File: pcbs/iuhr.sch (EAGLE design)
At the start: 70 parts, among them IC1 TPS77033, IC2 MEGA48/88/168-AU, Q1 20.000MHz

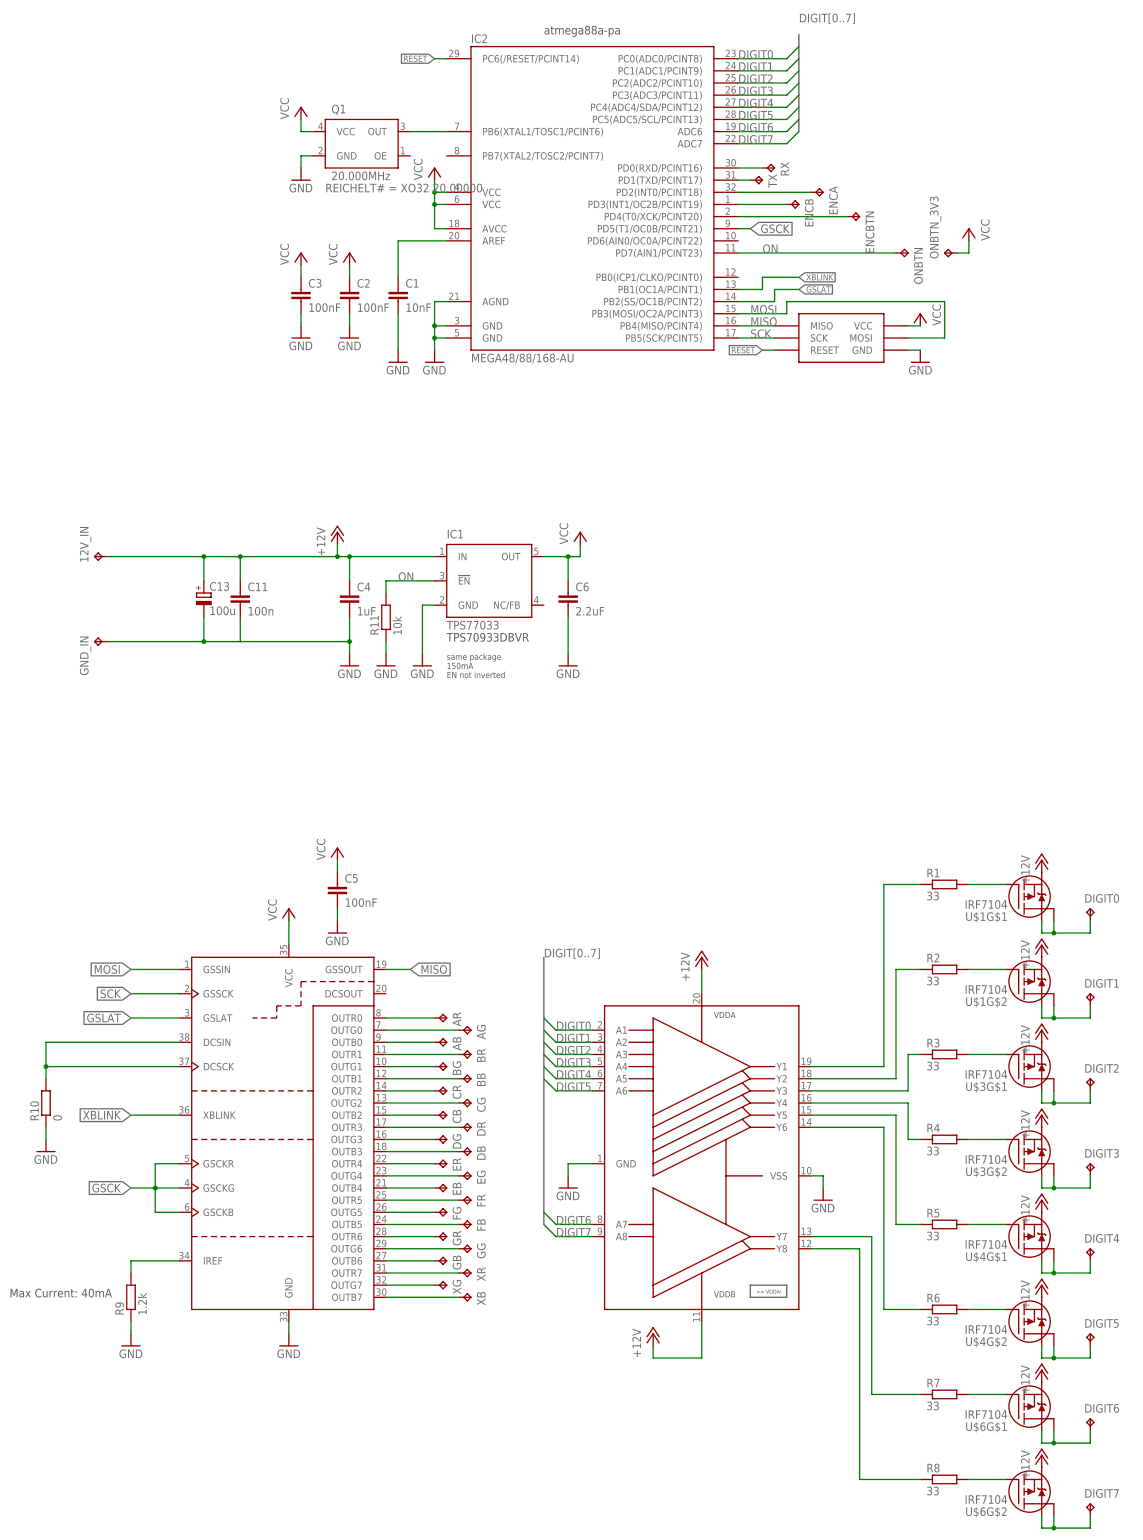
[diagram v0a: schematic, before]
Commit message: Started board layout
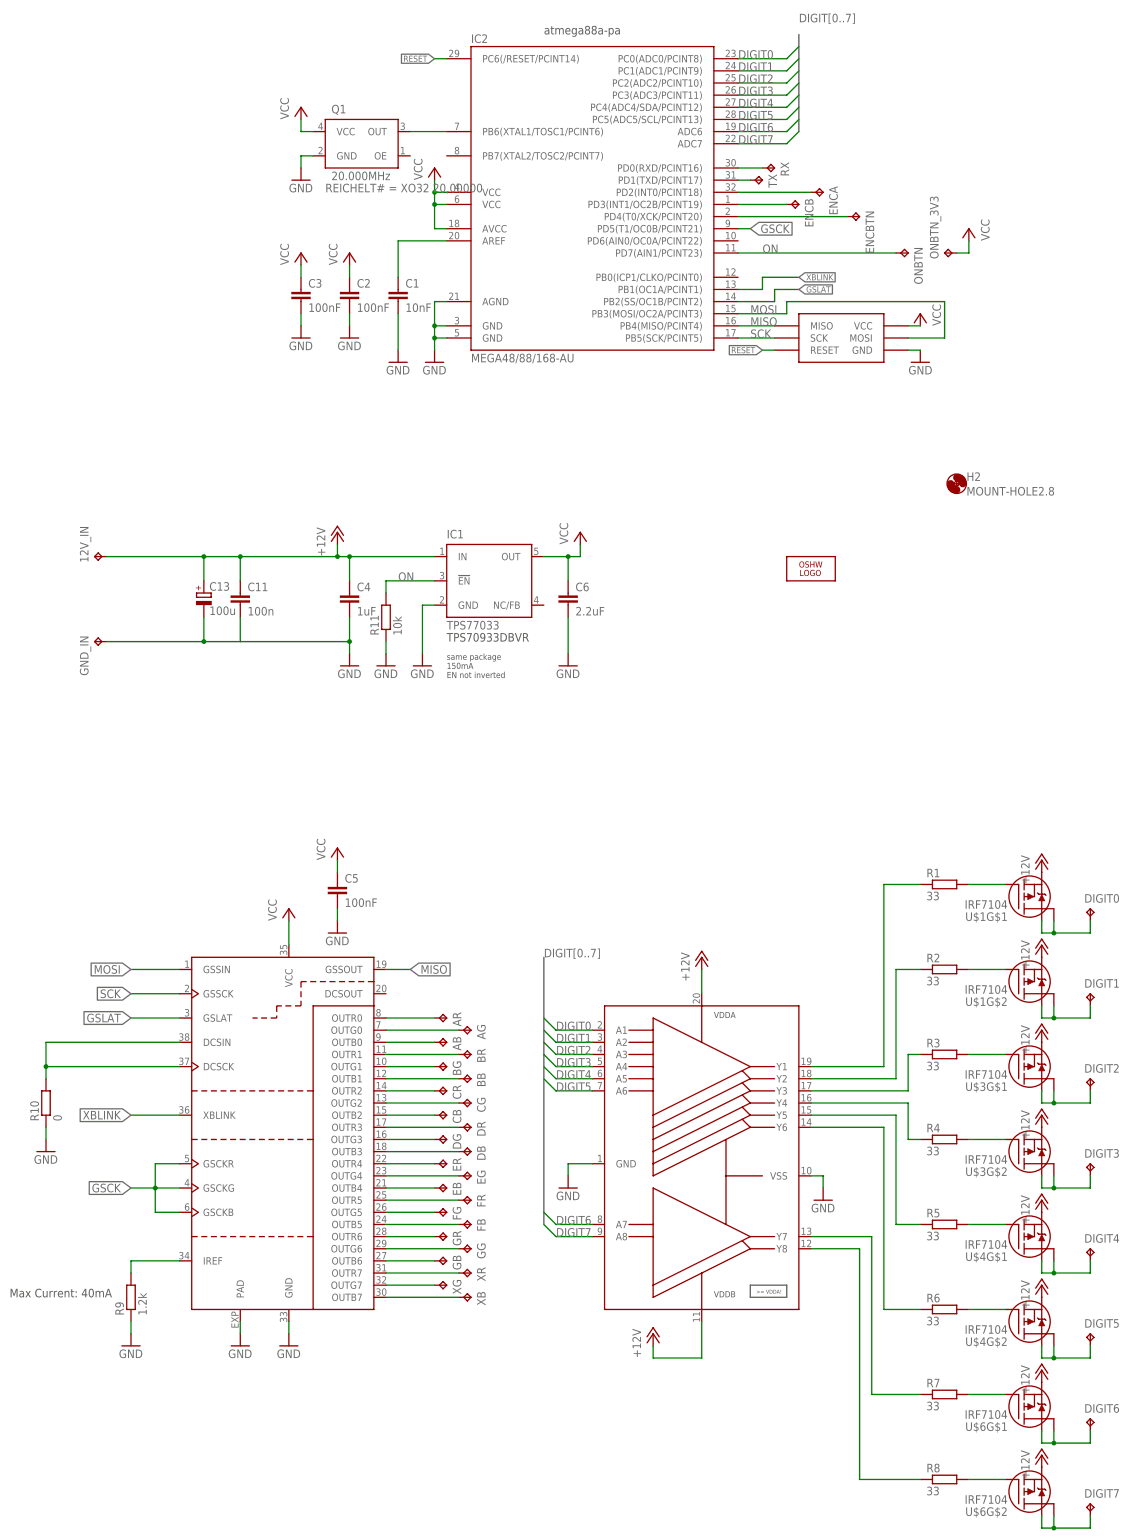
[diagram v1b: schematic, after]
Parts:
- added H2: MOUNT-HOLE2.8, holes:MOUNT-HOLE2.8
- added LOGO2: OSHW_LOGO_8MILX0150-NT, ea:OSHW_LOGO_8MILX0150-NT
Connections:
- net GND: now also DAP1.PAD
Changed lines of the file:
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@@
 <part name="P+20" library="supply1" deviceset="VCC" device=""/>
 <part name="GND15" library="supply1" deviceset="GND" device=""/>
+<part name="H2" library="holes" deviceset="MOUNT-HOLE" device="2.8"/>
+<part name="GND16" library="supply1" deviceset="GND" device=""/>
+<part name="LOGO2" library="ea" deviceset="OSHW_LOGO_8MIL" device="X0150-NT"/>
 </parts>
 <sheets>
@@
 <instance part="P+20" gate="VCC" x="88.9" y="-12.7"/>
 <instance part="GND15" gate="1" x="88.9" y="-30.48"/>
+<instance part="H2" gate="G$1" x="218.44" y="63.5"/>
+<instance part="GND16" gate="1" x="68.58" y="-116.84"/>
+<instance part="LOGO2" gate="G$1" x="187.96" y="45.72"/>
 </instances>
 <busses>
@@
 <wire x1="88.9" y1="-27.94" x2="88.9" y2="-25.4" width="0.1524" layer="91"/>
 </segment>
+<segment>
+<pinref part="DAP1" gate="G$1" pin="PAD"/>
+<pinref part="GND16" gate="1" pin="GND"/>
+<wire x1="68.58" y1="-114.3" x2="68.58" y2="-111.76" width="0.1524" layer="91"/>
+</segment>
 </net>

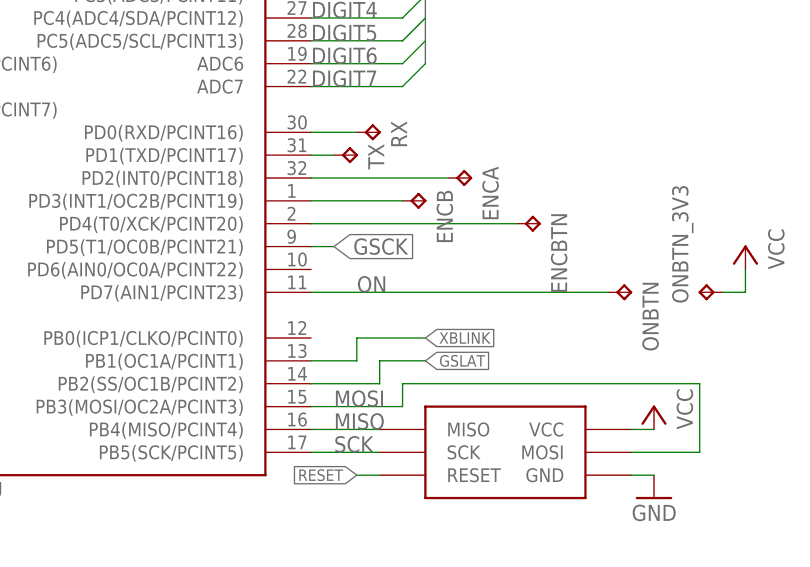
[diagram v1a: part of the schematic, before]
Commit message: No Airwires. No unapproved DRC Errors.
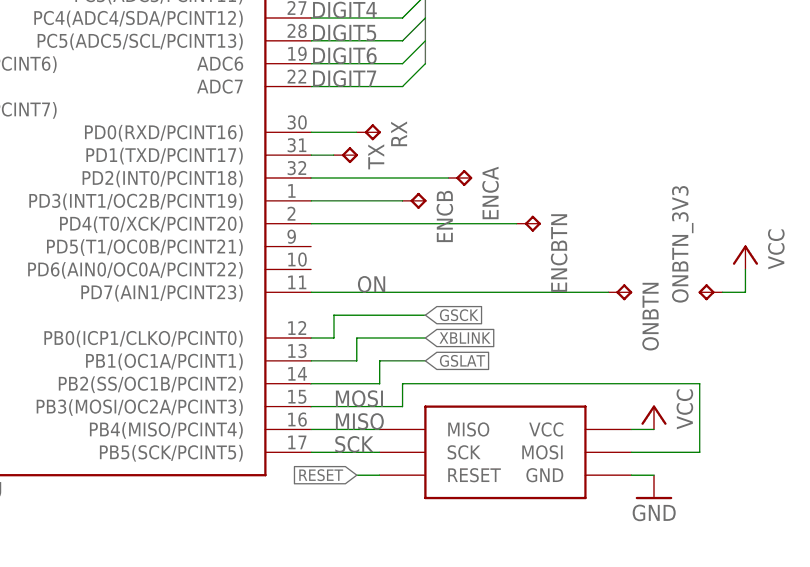
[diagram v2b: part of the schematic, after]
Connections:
- net GSCK: now also IC2.PB0(ICP1/CLKO/PCINT0); no longer IC2.PD5(T1/OC0B/PCINT21)
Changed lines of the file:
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@@
 </segment>
 <segment>
-<pinref part="IC2" gate="1" pin="PD5(T1/OC0B/PCINT21)"/>
-<wire x1="172.72" y1="116.84" x2="175.26" y2="116.84" width="0.1524" layer="91"/>
-<label x="175.26" y="116.84" size="1.778" layer="95" xref="yes"/>
+<pinref part="IC2" gate="1" pin="PB0(ICP1/CLKO/PCINT0)"/>
+<wire x1="172.72" y1="106.68" x2="175.26" y2="106.68" width="0.1524" layer="91"/>
+<wire x1="175.26" y1="106.68" x2="175.26" y2="109.22" width="0.1524" layer="91"/>
+<wire x1="175.26" y1="109.22" x2="185.42" y2="109.22" width="0.1524" layer="91"/>
+<label x="185.42" y="109.22" size="1.27" layer="95" xref="yes"/>
 </segment>
 </net>

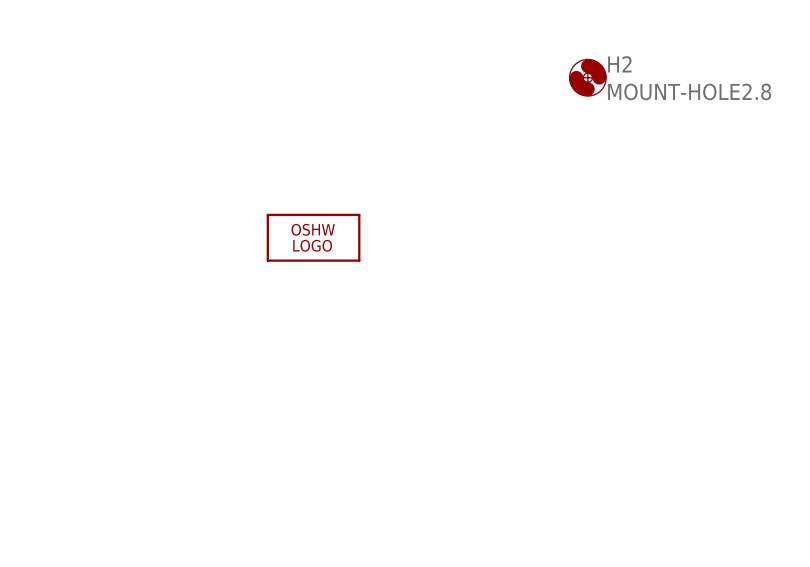
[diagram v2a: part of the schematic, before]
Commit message: Add ground plane and thermal vias.
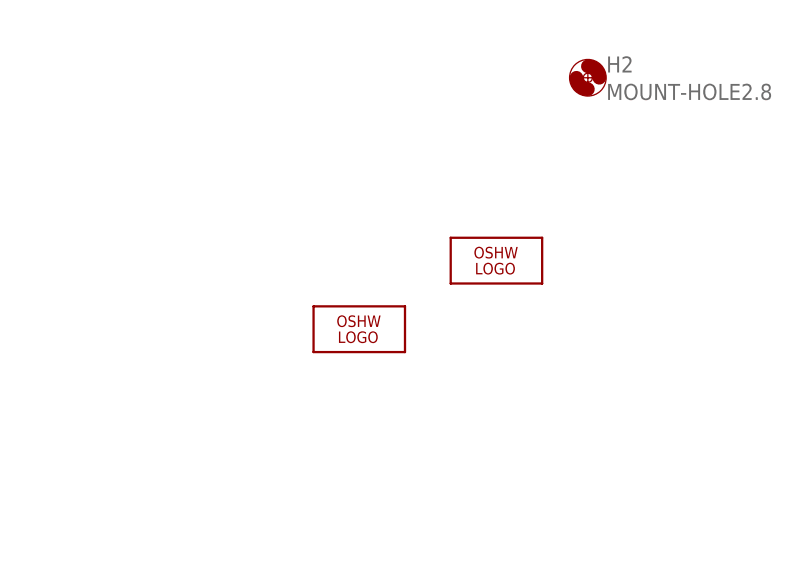
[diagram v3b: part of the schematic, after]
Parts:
- removed LOGO2: OSHW_LOGO_8MILX0150-NT, ea:OSHW_LOGO_8MILX0150-NT
- added LOGO1: OSHW_LOGO_8MILX0200-NT, ea:OSHW_LOGO_8MILX0200-NT
- added LOGO3: OSHW_LOGO_8MILX0350-NT, ea:OSHW_LOGO_8MILX0350-NT
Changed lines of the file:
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@@
 <part name="H2" library="holes" deviceset="MOUNT-HOLE" device="2.8"/>
 <part name="GND16" library="supply1" deviceset="GND" device=""/>
-<part name="LOGO2" library="ea" deviceset="OSHW_LOGO_8MIL" device="X0150-NT"/>
+<part name="LOGO1" library="ea" deviceset="OSHW_LOGO_8MIL" device="X0200-NT"/>
+<part name="LOGO3" library="ea" deviceset="OSHW_LOGO_8MIL" device="X0350-NT"/>
 </parts>
 <sheets>
@@
 <instance part="H2" gate="G$1" x="218.44" y="63.5"/>
 <instance part="GND16" gate="1" x="68.58" y="-116.84"/>
-<instance part="LOGO2" gate="G$1" x="187.96" y="45.72"/>
+<instance part="LOGO1" gate="G$1" x="208.28" y="43.18"/>
+<instance part="LOGO3" gate="G$1" x="193.04" y="35.56"/>
 </instances>
 <busses>

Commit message: Improved Silkscreen.
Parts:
- removed LOGO3: OSHW_LOGO_8MILX0350-NT, ea:OSHW_LOGO_8MILX0350-NT
- renumbered DAP1 to TLC5951, IC2 to ATMEGA88PA, U$1 to IRF7104, U$2 to ADG3123

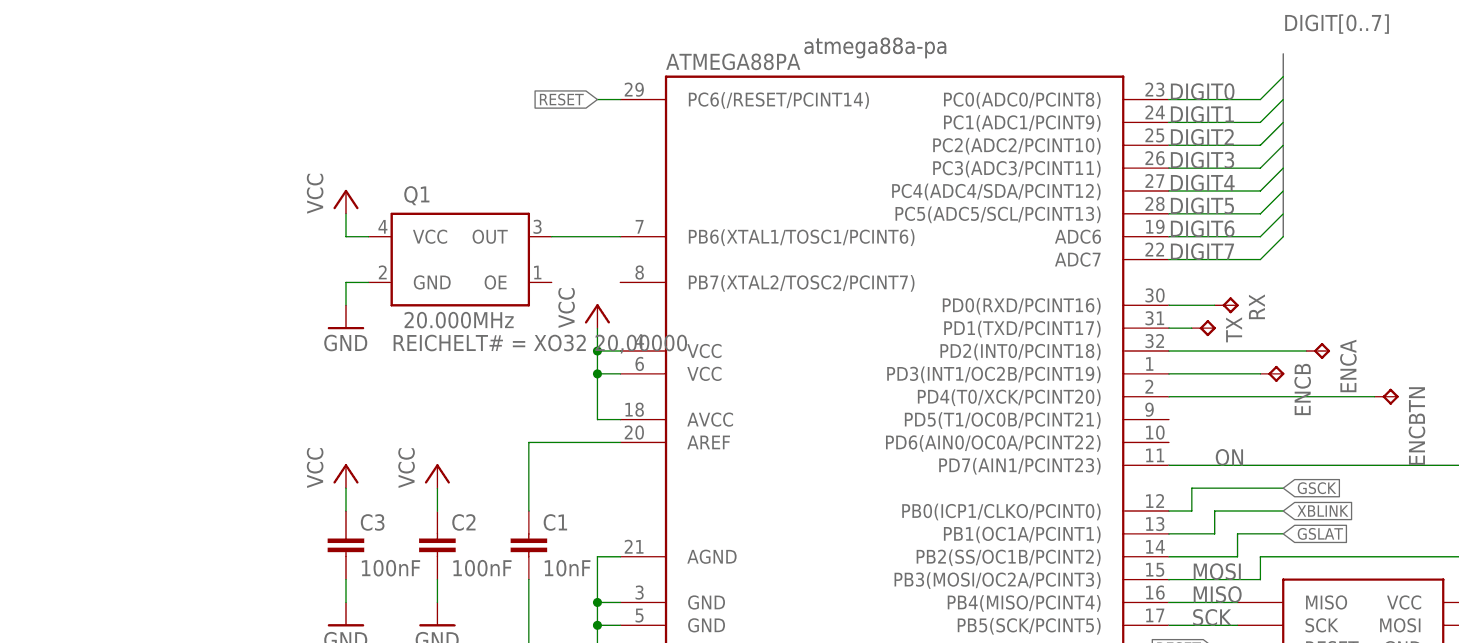
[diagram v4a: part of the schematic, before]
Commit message: Break out unused pins
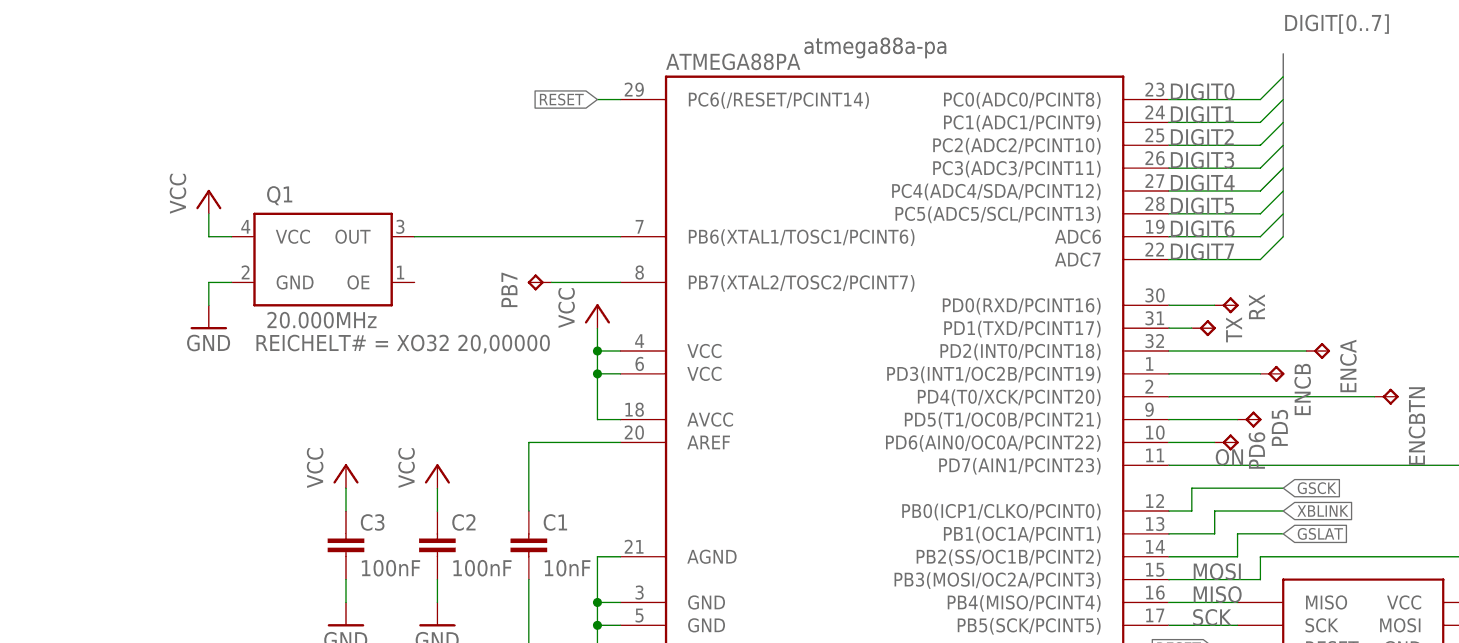
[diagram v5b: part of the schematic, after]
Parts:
- added PB7, PD5, PD6: TPTP15SQ, testpad:TPTP15SQ
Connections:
- new net N$56: ATMEGA88PA.PD5(T1/OC0B/PCINT21), PD5.TP
- new net N$57: ATMEGA88PA.PD6(AIN0/OC0A/PCINT22), PD6.TP
- new net N$58: ATMEGA88PA.PB7(XTAL2/TOSC2/PCINT7), PB7.TP
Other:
- moved on the sheet: Q1
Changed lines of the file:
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@@
 <part name="GND16" library="supply1" deviceset="GND" device=""/>
 <part name="LOGO1" library="ea" deviceset="OSHW_LOGO_8MIL" device="X0200-NT"/>
+<part name="PD6" library="testpad" deviceset="TP" device="TP15SQ"/>
+<part name="PD5" library="testpad" deviceset="TP" device="TP15SQ"/>
+<part name="PB7" library="testpad" deviceset="TP" device="TP15SQ"/>
 </parts>
 <sheets>
@@
 <instance part="ENCB" gate="G$1" x="185.42" y="121.92" rot="R270"/>
 <instance part="ENCBTN" gate="G$1" x="198.12" y="119.38" rot="R270"/>
-<instance part="Q1" gate="G$1" x="93.98" y="134.62">
-<attribute name="REICHELT#" x="86.36" y="124.46" size="1.778" layer="96" display="both"/>
+<instance part="Q1" gate="G$1" x="78.74" y="134.62">
+<attribute name="REICHELT#" x="71.12" y="124.46" size="1.778" layer="96" display="both"/>
 </instance>
-<instance part="GND32" gate="1" x="81.28" y="127"/>
-<instance part="P+18" gate="VCC" x="81.28" y="142.24"/>
+<instance part="GND32" gate="1" x="66.04" y="127"/>
+<instance part="P+18" gate="VCC" x="66.04" y="142.24"/>
 <instance part="ONBTN" gate="G$1" x="208.28" y="111.76" rot="R270"/>
 <instance part="ONBTN_3V3" gate="G$1" x="215.9" y="111.76" rot="R90"/>
@@
 <instance part="GND16" gate="1" x="68.58" y="-116.84"/>
 <instance part="LOGO1" gate="G$1" x="208.28" y="43.18"/>
+<instance part="PD6" gate="G$1" x="180.34" y="114.3" rot="R270"/>
+<instance part="PD5" gate="G$1" x="182.88" y="116.84" rot="R270"/>
+<instance part="PB7" gate="G$1" x="101.6" y="132.08" rot="MR270"/>
 </instances>
 <busses>
@@
 </segment>
 <segment>
-<wire x1="83.82" y1="132.08" x2="81.28" y2="132.08" width="0.1524" layer="91"/>
-<wire x1="81.28" y1="132.08" x2="81.28" y2="129.54" width="0.1524" layer="91"/>
+<wire x1="68.58" y1="132.08" x2="66.04" y2="132.08" width="0.1524" layer="91"/>
+<wire x1="66.04" y1="132.08" x2="66.04" y2="129.54" width="0.1524" layer="91"/>
 <pinref part="Q1" gate="G$1" pin="GND"/>
 <pinref part="GND32" gate="1" pin="GND"/>
@@
 </segment>
 <segment>
-<wire x1="83.82" y1="137.16" x2="81.28" y2="137.16" width="0.1524" layer="91"/>
-<wire x1="81.28" y1="137.16" x2="81.28" y2="139.7" width="0.1524" layer="91"/>
+<wire x1="68.58" y1="137.16" x2="66.04" y2="137.16" width="0.1524" layer="91"/>
+<wire x1="66.04" y1="137.16" x2="66.04" y2="139.7" width="0.1524" layer="91"/>
 <pinref part="Q1" gate="G$1" pin="VCC"/>
 <pinref part="P+18" gate="VCC" pin="VCC"/>
@@
 <net name="CLK_STM" class="0">
 <segment>
-<wire x1="104.14" y1="137.16" x2="111.76" y2="137.16" width="0.1524" layer="91"/>
+<wire x1="88.9" y1="137.16" x2="111.76" y2="137.16" width="0.1524" layer="91"/>
 <pinref part="Q1" gate="G$1" pin="OUT"/>
 <pinref part="ATMEGA88PA" gate="1" pin="PB6(XTAL1/TOSC1/PCINT6)"/>
 </segment>
 </net>
+<net name="N$56" class="0">
+<segment>
+<pinref part="ATMEGA88PA" gate="1" pin="PD5(T1/OC0B/PCINT21)"/>
+<wire x1="172.72" y1="116.84" x2="180.34" y2="116.84" width="0.1524" layer="91"/>
+<pinref part="PD5" gate="G$1" pin="TP"/>
+</segment>
+</net>
+<net name="N$57" class="0">
+<segment>
+<pinref part="ATMEGA88PA" gate="1" pin="PD6(AIN0/OC0A/PCINT22)"/>
+<wire x1="172.72" y1="114.3" x2="177.8" y2="114.3" width="0.1524" layer="91"/>
+<pinref part="PD6" gate="G$1" pin="TP"/>
+</segment>
+</net>
+<net name="N$58" class="0">
+<segment>
+<pinref part="ATMEGA88PA" gate="1" pin="PB7(XTAL2/TOSC2/PCINT7)"/>
+<pinref part="PB7" gate="G$1" pin="TP"/>
+<wire x1="104.14" y1="132.08" x2="111.76" y2="132.08" width="0.1524" layer="91"/>
+</segment>
+</net>
